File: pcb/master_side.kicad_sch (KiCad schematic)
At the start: 109 parts, among them IC1 PCA9956BTWY, J2 4P4C, J4 USB_C_Receptacle_USB2.0_16P, SW1 SW_Push_45deg, SW10 SW_Push_45deg, SW11 SW_Push_45deg, SW12 SW_Push_45deg, SW13 SW_Push_45deg, SW14 SW_Push_45deg, SW15 SW_Push_45deg, SW16 SW_Push_45deg, SW17 SW_Push_45deg, SW18 SW_Push_45deg, SW2 SW_Push_45deg, SW3 SW_Push_45deg, SW4 SW_Push_45deg, SW5 SW_Push_45deg, SW6 SW_Push_45deg, SW7 SW_Push_45deg, SW8 SW_Push_45deg, SW9 SW_Push_45deg, U1 W25Q128JVSIQ, U2 RP2040, U3 NCP1117LPST33T3G, U4 OPT3001DNPR, Y1 ABM8-272-T3

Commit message: fix(left side): Made power traces wider, simplified W25Q128 storage interrupt switch routing with vias to 3.3V
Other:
- note added: "same I2C adress as the LED driver on slave side, but using different I2C bus, so no conflict"
- note removed: "same I2C adress as the LED driver on master side, but using different I2C bus, so no conflict"
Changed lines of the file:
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@@
 		)
 	)
-	(text "same I2C adress as the LED driver on master side, \nbut using different I2C bus, so no conflict"
+	(text "same I2C adress as the LED driver on slave side, \nbut using different I2C bus, so no conflict"
 		(exclude_from_sim no)
 		(at 53.34 185.42 0)

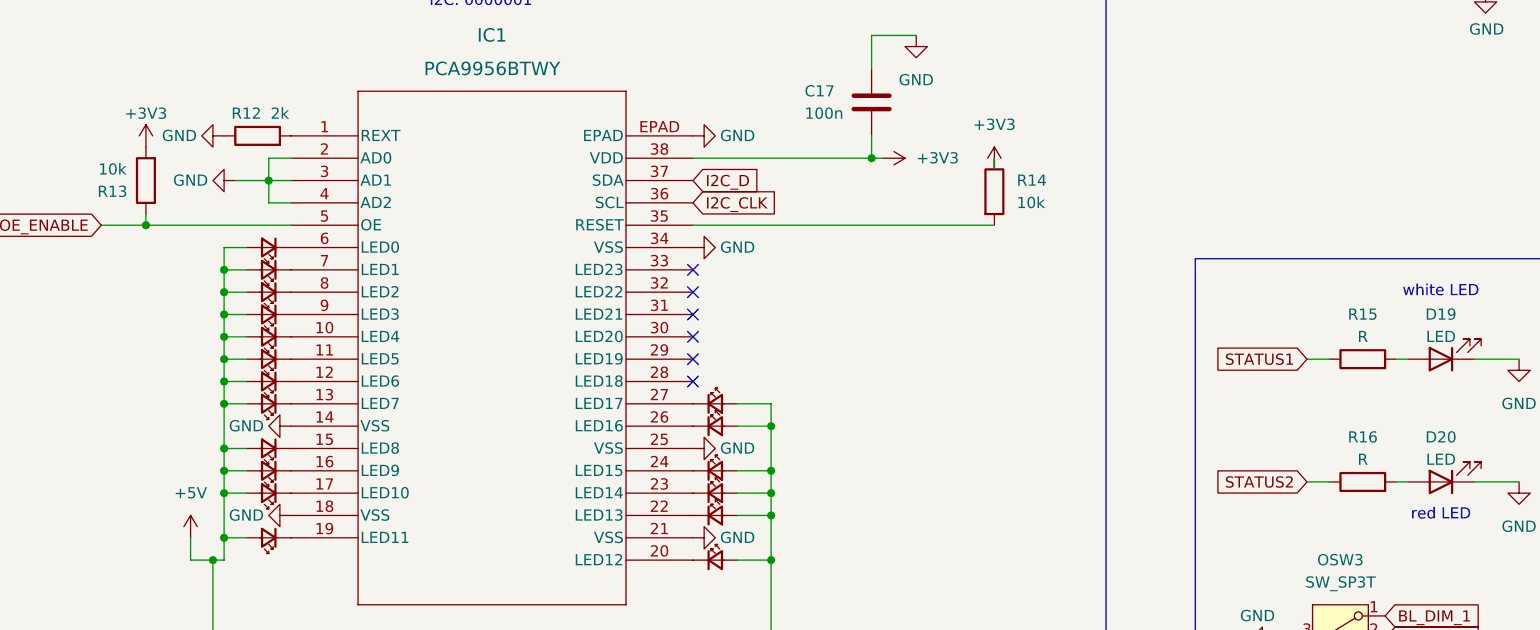
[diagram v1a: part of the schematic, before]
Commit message: feat: Add screw mount holes, add more JLC part numbers, fix DRC violations, remove all components at least 1mm from the edge of the board, add Cherry switch 3D model to ai03 footprint
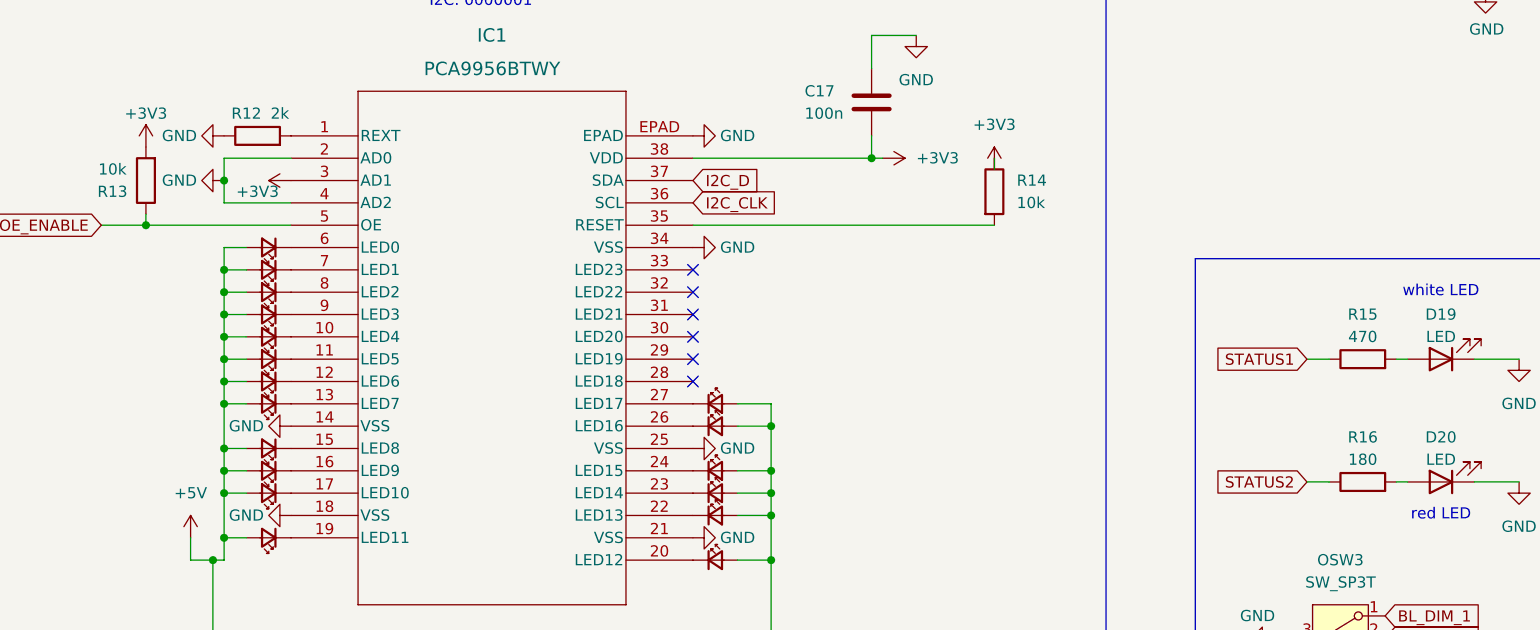
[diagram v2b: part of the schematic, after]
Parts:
- R15: value R -> 470
- R16: value R -> 180
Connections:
- net +3V3: now also IC1.3 (AD1)
- net GND: no longer IC1.3 (AD1)
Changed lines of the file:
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@@
 	)
 	(junction
-		(at 55.88 212.09)
-		(diameter 0)
-		(color 0 0 0 0)
-	)
-	(junction
 		(at 104.14 100.33)
 		(diameter 0)
@@
 	)
 	(junction
+		(at 50.8 212.09)
+		(diameter 0)
+		(color 0 0 0 0)
+	)
+	(junction
 		(at 50.8 242.57)
 		(diameter 0)
@@
 	(wire
 		(pts
-			(xy 52.07 212.09) (xy 55.88 212.09)
-		)
-		(stroke
-			(width 0)
-			(type default)
-		)
-	)
-	(wire
-		(pts
 			(xy 389.89 57.15) (xy 397.51 57.15)
 		)
@@
 	(wire
 		(pts
-			(xy 55.88 209.55) (xy 58.42 209.55)
+			(xy 50.8 209.55) (xy 58.42 209.55)
 		)
 		(stroke
@@
 	(wire
 		(pts
-			(xy 58.42 214.63) (xy 55.88 214.63)
+			(xy 58.42 214.63) (xy 50.8 214.63)
 		)
 		(stroke
@@
 	(wire
 		(pts
-			(xy 55.88 214.63) (xy 55.88 212.09)
+			(xy 50.8 214.63) (xy 50.8 212.09)
 		)
 		(stroke
@@
 	(wire
 		(pts
-			(xy 55.88 212.09) (xy 58.42 212.09)
-		)
-		(stroke
-			(width 0)
-			(type default)
-		)
-	)
-	(wire
-		(pts
 			(xy 50.8 219.71) (xy 53.34 219.71)
 		)
@@
 	(wire
 		(pts
-			(xy 55.88 212.09) (xy 55.88 209.55)
+			(xy 50.8 212.09) (xy 50.8 209.55)
 		)
 		(stroke
@@
 			)
 		)
-		(property "Value" "R"
+		(property "Value" "180"
 			(at 180.34 243.84 90)
 			(show_name no)
@@
 			)
 		)
-		(property "Value" "R"
+		(property "Value" "470"
 			(at 180.34 229.87 90)
 			(show_name no)
@@
 		(lib_name "GND_2")
 		(lib_id "power:GND")
-		(at 52.07 212.09 270)
+		(at 50.8 212.09 270)
 		(unit 1)
 		(body_style 1)
@@
 		(dnp no)
 		(property "Reference" "#PWR036"
-			(at 45.72 212.09 0)
+			(at 44.45 212.09 0)
 			(hide yes)
 			(show_name no)
@@
 		)
 		(property "Value" "GND"
-			(at 46.99 212.09 90)
+			(at 45.72 212.09 90)
 			(show_name no)
 			(do_not_autoplace no)
@@
 		)
 		(property "Footprint" ""
-			(at 52.07 212.09 0)
+			(at 50.8 212.09 0)
 			(hide yes)
 			(show_name no)
@@
 		)
 		(property "Datasheet" ""
-			(at 52.07 212.09 0)
+			(at 50.8 212.09 0)
 			(hide yes)
 			(show_name no)
@@
 		)
 		(property "Description" "Power symbol creates a global label with name \"GND\" , ground"
-			(at 52.07 212.09 0)
+			(at 50.8 212.09 0)
 			(hide yes)
 			(show_name no)
@@
 					(unit 1)
 				)
+			)
+		)
+	)
+	(symbol
+		(lib_id "power:+3V3")
+		(at 58.42 212.09 90)
+		(unit 1)
+		(body_style 1)
+		(exclude_from_sim no)
+		(in_bom yes)
+		(on_board yes)
+		(in_pos_files yes)
+		(dnp no)
+		(property "Reference" "#PWR061"
+			(at 62.23 212.09 0)
+			(hide yes)
+			(show_name no)
+			(do_not_autoplace no)
+			(effects
+				(font
+					(size 1.27 1.27)
+				)
+			)
+		)
+		(property "Value" "+3V3"
+			(at 54.61 213.36 90)
+			(show_name no)
+			(do_not_autoplace no)
+			(effects
+				(font
+					(size 1.27 1.27)
+				)
+			)
+		)
+		(property "Footprint" ""
+			(at 58.42 212.09 0)
+			(hide yes)
+			(show_name no)
+			(do_not_autoplace no)
+			(effects
+				(font
+					(size 1.27 1.27)
+				)
+			)
+		)
+		(property "Datasheet" ""
+			(at 58.42 212.09 0)
+			(hide yes)
+			(show_name no)
+			(do_not_autoplace no)
+			(effects
+				(font
+					(size 1.27 1.27)
+				)
+			)
+		)
+		(property "Description" "Power symbol creates a global label with name \"+3V3\""
+			(at 58.42 212.09 0)
+			(hide yes)
+			(show_name no)
+			(do_not_autoplace no)
+			(effects
+				(font
+					(size 1.27 1.27)
+				)
+			)
+		)
+		(pin "1"
+		)
+		(instances
+			(project "mSCKee"
+				(path "/2ec7cb33-7d00-426e-b710-cc42b1f2f810/e8479b67-c66f-4a93-9ef2-59ef63eac199"
+					(reference "#PWR061")
+					(unit 1)
+				)

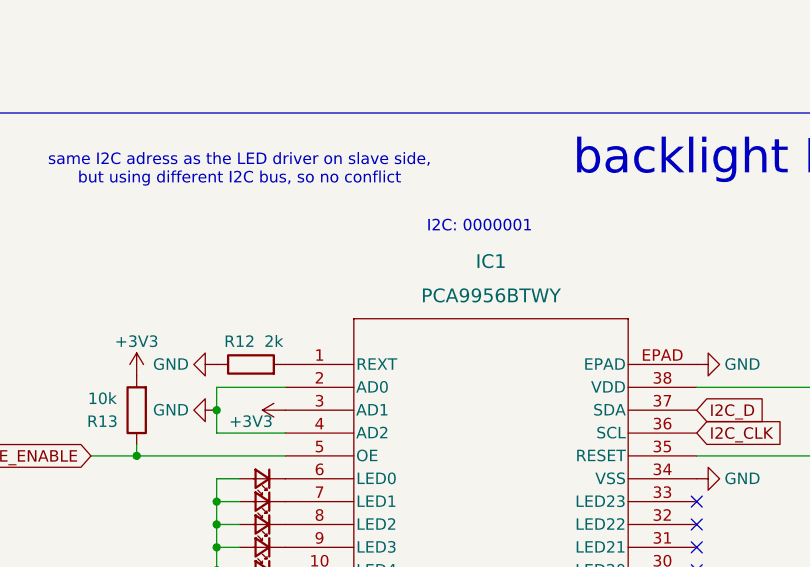
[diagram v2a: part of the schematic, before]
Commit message: fix: Size all footprints on the back side 0805 for hand soldering
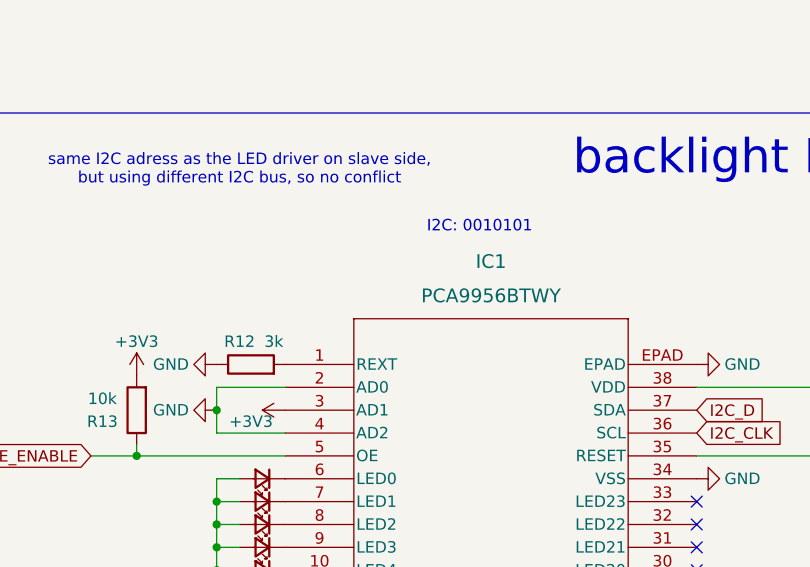
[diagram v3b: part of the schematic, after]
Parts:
- R12: value 2k -> 3k
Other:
- note added: "I2C: 0010101"
- note removed: "I2C: 0000001"
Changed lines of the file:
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@@
 		)
 	)
-	(text "I2C: 0000001"
+	(text "I2C: 0010101"
 		(exclude_from_sim no)
 		(at 80.01 191.77 0)
@@
 			)
 		)
-		(property "Value" "2k"
+		(property "Value" "3k"
 			(at 57.15 204.47 90)
 			(show_name no)
